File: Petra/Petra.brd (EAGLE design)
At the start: 98.1 x 38.1 mm, 37 parts, among them J2 AVR_SPI_PRG_6NS, U1 MIC5219 5V, Y1 16MHz

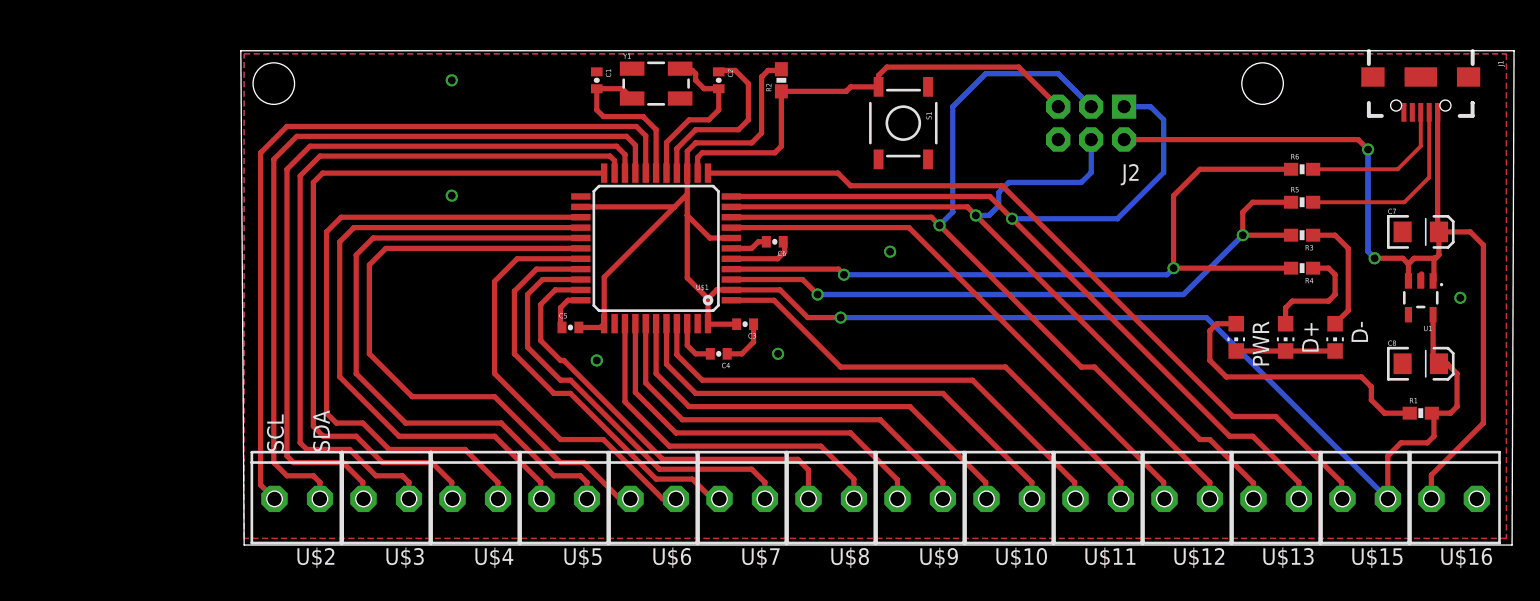
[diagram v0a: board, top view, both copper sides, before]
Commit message: Made screw terminal board smaller. Added BOM for Petra
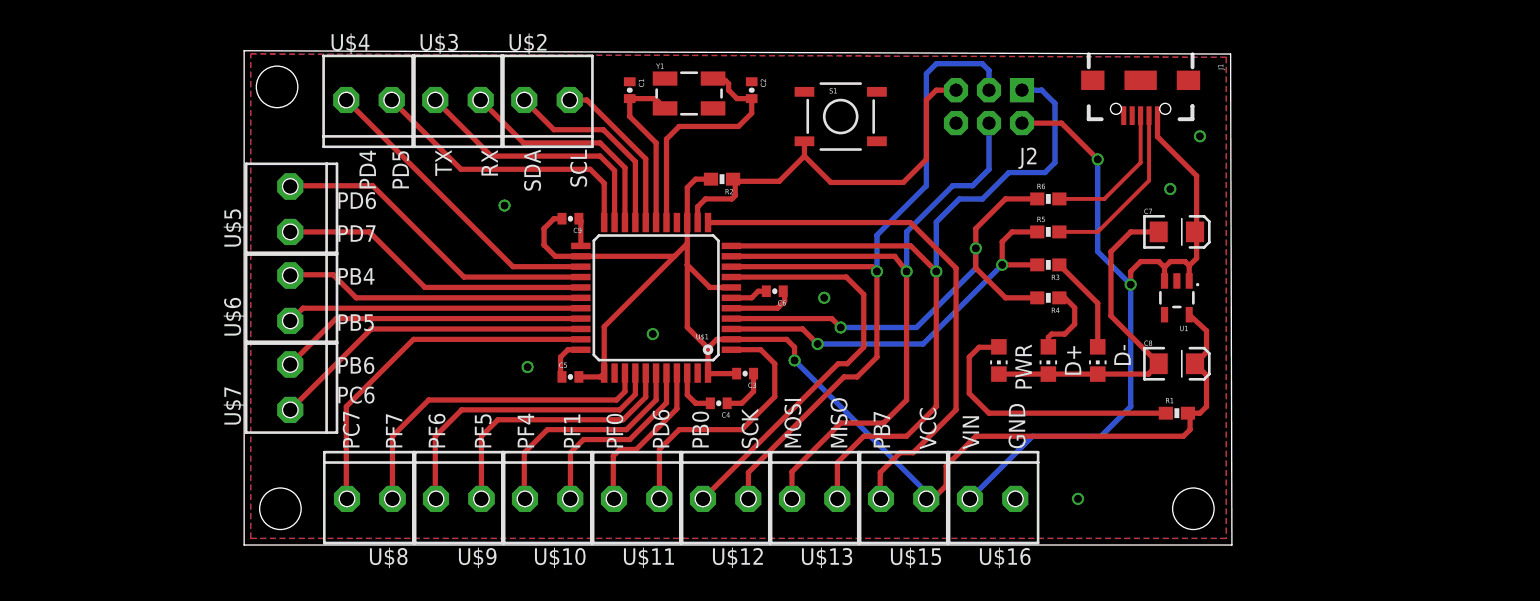
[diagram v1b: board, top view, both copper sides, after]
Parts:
- added C9: 1uF, SparkFun-Passives:0402-CAP
- moved U$7 37.2 mm to (3.56, 10.4), turned to 90 degrees
- moved U$10 35.6 mm to (25.1, 3.56)
- moved U$13 35.6 mm to (45.7, 3.56)
- moved U$15 35.6 mm to (52.6, 3.56)
- moved U$8 35.6 mm to (11.4, 3.56)
- moved U$9 35.6 mm to (18.3, 3.56)
- moved U$11 35.6 mm to (32.0, 3.56)
- moved U$12 35.6 mm to (38.9, 3.56)
- moved U$16 35.6 mm to (59.4, 3.56)
- moved U$2 34.5 mm to (21.6, 34.3), turned to 0 degrees
- moved U$4 32.9 mm to (7.87, 34.3), turned to 0 degrees
- moved U$6 32.7 mm to (3.56, 17.3), turned to 90 degrees
- moved U$3 30.8 mm to (14.7, 34.3), turned to 0 degrees
- moved U$5 30.8 mm to (3.56, 24.1), turned to 90 degrees
- moved J1 21.6 mm to (69.1, 35.8)
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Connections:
- net GND: now also C9.1
- net VCC: now also C9.2
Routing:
- net SCL: track 60.8 -> 12.6 mm
- net SDA: track 59.9 -> 15.2 mm
- net RX: track 58.6 -> 17.5 mm
- net TX: track 57.5 -> 20.1 mm
- net PD5: track 55.3 -> 22.1 mm
- net PD4: track 50.7 -> 23.4 mm
- net PF0: track 38.4 -> 12.5 mm
- net PD7: track 49.5 -> 24.2 mm
- net PB4: track 48.4 -> 23.2 mm
- net PD6: track 49.6 -> 25.3 mm
- net VCC: track 133.7 -> 109.4 mm
- net D+: track 59.0 -> 37.0 mm
- net PF1: track 36.3 -> 14.8 mm
- net D-: track 51.3 -> 31.4 mm
- net PB7: track 60.0 -> 41.4 mm
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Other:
- board size 98.1 x 38.1 mm -> 76.1 x 38.1 mm
- board text added: "GND"
- board text added: "MISO"
- board text added: "MOSI"
- board text added: "PB0"
- board text added: "PB4"
- board text added: "PB5"
- board text added: "PB6"
- board text added: "PB7"
- board text added: "PC6"
- board text added: "PC7"
- board text added: "PD4"
- board text added: "PD5"
- board text added: "PD6"
- board text added: "PD7"
- board text added: "PF0"
- board text added: "PF1"
- board text added: "PF4"
- board text added: "PF5"
- board text added: "PF6"
- board text added: "PF7"
- board text added: "RX"
- board text added: "SCK"
- board text added: "TX"
- board text added: "VCC"
- board text added: "VIN"

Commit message: moving to 20 pin io connector
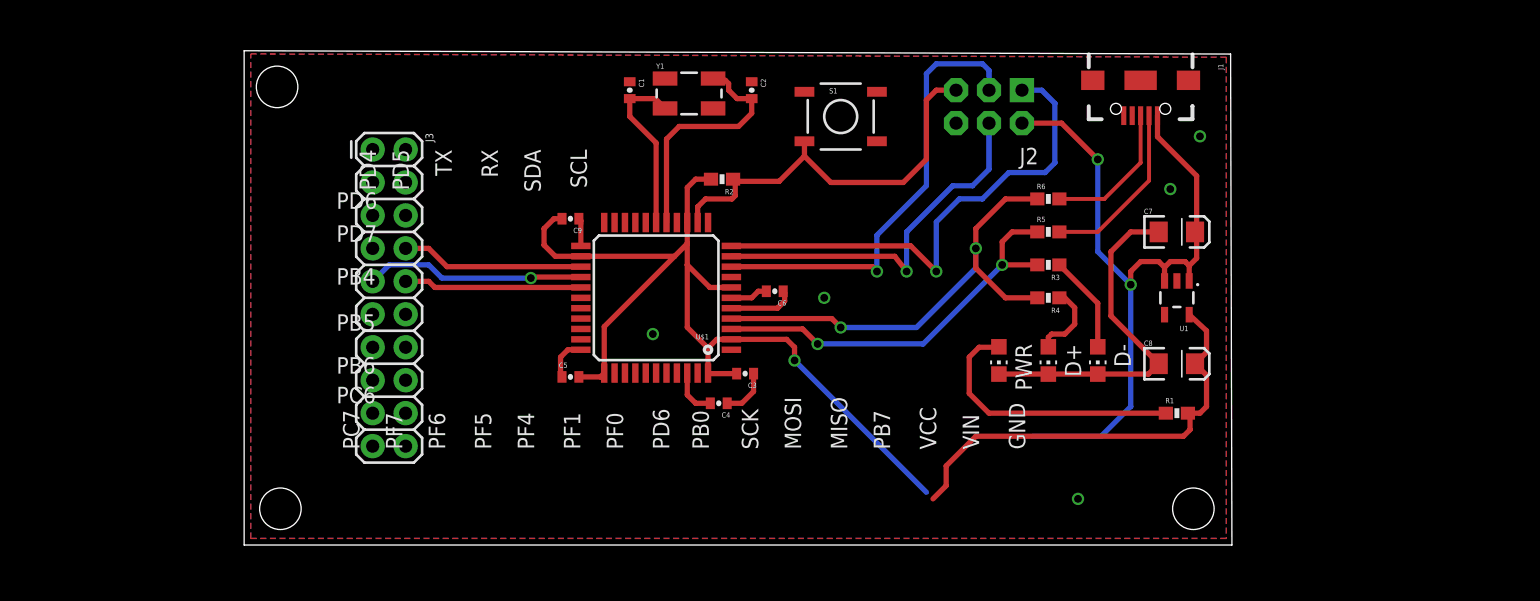
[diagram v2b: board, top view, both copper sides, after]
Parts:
- removed U$10, U$11, U$12, U$13, U$15, U$16, U$2, U$3, U$4, U$5, U$6, U$7, U$8, U$9: SCREW_1X2, PartsYouNeed:1X2-SCREW
- added J3: (no value), SparkFun-Connectors:2X10
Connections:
- net GND: no longer U$16.1
- net MISO: no longer U$13.1
- net MOSI: no longer U$13.2
- net PB0: now also J3.3; no longer U$12.2
- net PB4: now also J3.11; no longer U$6.2
- net PB5: now also J3.12; no longer U$6.1
- net PB6: now also J3.13; no longer U$7.2
- net PB7: now also J3.1; no longer U$15.2
- net PC6: now also J3.14; no longer U$7.1
- net PC7: now also J3.15; no longer U$8.2
- net PD4: now also J3.8; no longer U$4.1
- net PD5: now also J3.7; no longer U$4.2
- net PD6: now also J3.9; no longer U$5.2
- net PD7: now also J3.10; no longer U$5.1
- net PE6: now also J3.17; no longer U$11.1
- net PF0: now also J3.19; no longer U$11.2
- net PF1: now also J3.20; no longer U$10.1
- net PF4: now also J3.18; no longer U$10.2
- net PF5: no longer U$9.1
- net PF6: no longer U$9.2
- net PF7: now also J3.16; no longer U$8.1
- net RX: now also J3.5; no longer U$3.2
- net SCK: no longer U$12.1
- net SCL: now also J3.2; no longer U$2.2
- net SDA: now also J3.4; no longer U$2.1
- net TX: now also J3.6; no longer U$3.1
- net VCC: no longer U$15.1
- net VIN: no longer U$16.2
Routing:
- net PB7: track 41.4 -> 0.00 mm
- net PB0: track 32.1 -> 0.00 mm
- net PC7: track 27.4 -> 0.00 mm
- net PF7: track 25.6 -> 0.00 mm
- net PC6: track 25.0 -> 0.00 mm
- net PB6: track 23.9 -> 0.00 mm
- net PF6: track 23.2 -> 0.00 mm
- net PB4: track 23.2 -> 0.00 mm
- net MOSI: track 52.1 -> 29.0 mm
- net PB5: track 22.8 -> 0.00 mm
- net MISO: track 61.6 -> 39.0 mm
- net SCK: track 57.3 -> 35.1 mm
- net PD5: track 22.1 -> 0.00 mm
- net PE6: track 20.7 -> 0.00 mm
- net PF5: track 20.6 -> 0.00 mm
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
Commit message: Completed io change. Reduced board size
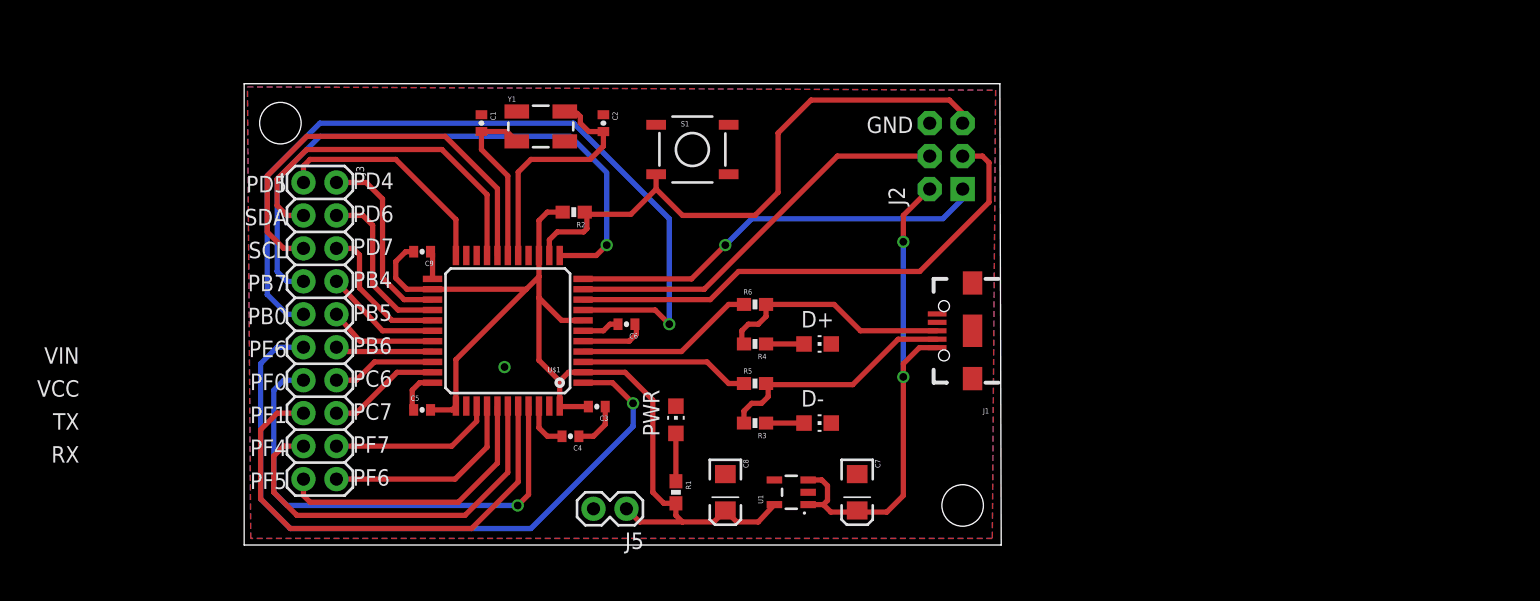
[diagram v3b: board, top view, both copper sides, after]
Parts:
- added J5: (no value), SparkFun-Connectors:1X02
- moved R1 39.1 mm to (33.3, 4.06), turned to 270 degrees
- moved C8 36.2 mm to (37.1, 4.06), turned to 270 degrees
- moved U1 33.3 mm to (42.2, 4.06), turned to 90 degrees
- moved C7 31.8 mm to (47.2, 4.06), turned to 270 degrees
- moved R3 25.7 mm to (39.4, 9.40)
- moved R5 25.4 mm to (39.4, 12.4)
- moved PWR 25.3 mm to (33.3, 9.65), turned to 0 degrees
- moved R6 24.0 mm to (39.4, 18.5)
- moved J1 23.2 mm to (56.1, 16.5), turned to 180 degrees
- moved R4 22.9 mm to (39.4, 15.5)
- moved D- 22.1 mm to (44.2, 9.40), turned to 270 degrees
- moved D+ 17.8 mm to (44.2, 15.5), turned to 270 degrees
- moved C5 11.7 mm to (13.7, 10.4)
- moved C9 11.7 mm to (13.7, 22.6)
- moved C1 11.7 mm to (18.3, 32.5)
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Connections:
- net D+: no longer R4.2
- net D-: no longer R3.2
- net GND: now also J5.2
- net N$5: now also R3.2
- net N$6: now also R4.2
- net PB0: now also J3.9; no longer J3.3
- net PB4: now also J3.8; no longer J3.11
- net PB5: now also J3.10; no longer J3.12
- net PB6: now also J3.12; no longer J3.13
- net PB7: now also J3.7; no longer J3.1
- net PC7: now also J3.16; no longer J3.15
- net PD4: now also J3.2; no longer J3.8
- net PD5: now also J3.1; no longer J3.7
- net PD6: now also J3.4; no longer J3.9
- net PD7: now also J3.6; no longer J3.10
- net PE6: now also J3.11; no longer J3.17
- net PF0: now also J3.13; no longer J3.19
- net PF1: now also J3.15; no longer J3.20
- net PF4: now also J3.17; no longer J3.18
- net PF5: now also J3.19
- net PF6: now also J3.20
- net PF7: now also J3.18; no longer J3.16
- net RX: no longer J3.5
- net SCL: now also J3.5; no longer J3.2
- net SDA: now also J3.3; no longer J3.4
- net TX: no longer J3.6
- net VCC: now also J5.1
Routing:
- net PB0: track 0.00 -> 63.5 mm, vias 0 -> 1
- net PE6: track 0.00 -> 53.4 mm, vias 0 -> 1
- net PB7: track 0.00 -> 46.9 mm, vias 0 -> 1
- net PF0: track 0.00 -> 37.7 mm, vias 0 -> 1
- net PF1: track 0.00 -> 37.3 mm
- net SCL: track 0.00 -> 33.5 mm
- net PF4: track 0.00 -> 30.7 mm
- net SDA: track 0.00 -> 27.6 mm
- net GND: track 41.6 -> 14.5 mm
- net VCC: track 108.4 -> 83.9 mm, vias 1 -> 0
- net D+: track 37.0 -> 13.9 mm, vias 2 -> 0
- net PF5: track 0.00 -> 22.1 mm
- net D-: track 31.4 -> 13.1 mm, vias 2 -> 0
- net PD5: track 0.00 -> 17.9 mm
- net N$7: track 21.2 -> 3.69 mm
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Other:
- board size 76.1 x 38.1 mm -> 58.3 x 35.5 mm
- board text added: "PE6"
- board text removed: "MISO"
- board text removed: "MOSI"
- board text removed: "SCK"

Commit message: Changed usb and button part. Reduced board size even further.
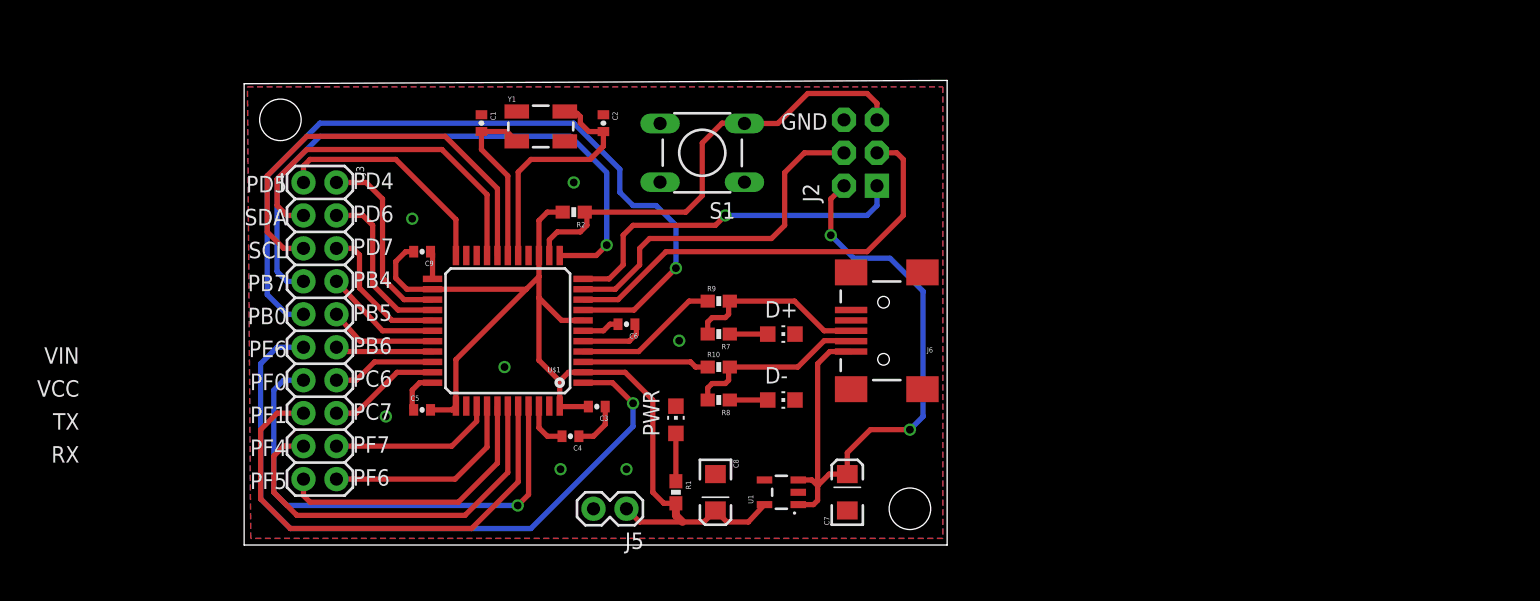
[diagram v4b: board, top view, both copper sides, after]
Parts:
- removed J1: (no value), SparkFun-Connectors:USB-B-MICRO-SMD_V03
- removed R3, R4: 1K, SparkFun-Resistors:0603-RES
- removed R5, R6: 22, SparkFun-Resistors:0603-RES
- added J6: USB-MINIB-5PIN, SparkFun-Connectors:USB-MINIB
- added R10, R9: 22, SparkFun-Resistors:0603-RES
- added R7, R8: 1K, SparkFun-Resistors:0603-RES
- S1: device SparkFun-Retired:TACTILE-SWITCH-SMD -> GeekAmmo:TAC-SWITCH-PTH
- moved J2 6.61 mm to (47.5, 30.2)
- moved D- 3.31 mm to (41.4, 11.2)
- moved D+ 2.90 mm to (41.4, 16.3)
- moved S1 0.80 mm to (35.3, 30.2), turned to 180 degrees
- moved C7 0.76 mm to (46.5, 4.06), turned to 90 degrees
- moved C8 0.76 mm to (36.3, 4.06)
- moved U1 0.76 mm to (41.4, 4.06)
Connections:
- removed net N$11: D-.A, R3.1
- removed net N$5: J1.D-, R3.2, R5.2
- removed net N$6: J1.D+, R4.2, R6.2
- removed net N$9: D+.A, R4.1
- new net N$27: D-.A, R8.1
- new net N$28: D+.A, R7.1
- new net N$29: J6.D+, R7.2, R9.2
- new net N$30: J6.D-, R10.2, R8.2
- net D+: now also R9.1; no longer R6.1
- net D-: now also R10.1; no longer R5.1
- net GND: now also J6.GND, J6.MTN1, J6.MTN2, J6.MTN3, J6.MTN4; no longer J1.GND, J1.SHIELD1, J1.SHIELD2, J1.SHIELD3
- net VIN: now also J6.VBUS; no longer J1.VBUS
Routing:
- net N$5: track 18.8 -> 0.00 mm, vias 0 -> 1
- net N$6: track 18.4 -> 0.00 mm
- net N$29: track 0.00 -> 14.1 mm
- net N$30: track 0.00 -> 14.0 mm
- net VIN: track 40.1 -> 50.9 mm
- net RST: track 45.1 -> 35.9 mm
- net SCK: track 39.7 -> 33.9 mm
- net MISO: track 32.6 -> 27.9 mm
- net MOSI: track 31.0 -> 27.6 mm
- net D-: track 13.1 -> 9.77 mm
- net N$9: track 2.93 -> 0.00 mm
- net N$11: track 2.93 -> 0.00 mm
- net N$28: track 0.00 -> 2.93 mm
- net N$27: track 0.00 -> 2.93 mm
- net D+: track 13.9 -> 11.2 mm
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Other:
- board size 58.3 x 35.5 mm -> 54.2 x 35.8 mm
